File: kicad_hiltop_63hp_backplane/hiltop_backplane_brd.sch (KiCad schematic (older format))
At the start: 0 parts

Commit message: PCI EXPRESS 96
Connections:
- wire segments 43 -> 53
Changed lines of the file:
@@
 	1600 6300 1600 6400
 $Comp
-L power:GND #PWR?
+L power:GND #PWR02
 U 1 1 5D0E934B
 P 1600 2600
-F 0 "#PWR?" H 1600 2350 50  0001 C CNN
+F 0 "#PWR02" H 1600 2350 50  0001 C CNN
 F 1 "GND" H 1600 2450 50  0000 C CNN
 F 2 "" H 1600 2600 50  0001 C CNN
@@
 F48 "LED6" I R 3700 2350 39
 F49 "LED7" I R 3700 2400 39
-$EndSheet
-$Sheet
-S 1700 3100 2000 2050
-U 5C074E5E
-F0 "MotherBoard_Connector" 60
-F1 "MotherBoard_Connector.sch" 60
-$EndSheet
-$Sheet
-S 8150 600  1750 5800
-U 5A0778ED
-F0 "backplane_connector" 60
-F1 "backplane_connector.sch" 60
-F2 "EXT_RESET" I L 8150 2350 39
-F3 "LVDS_D1-" I L 8150 2300 39
-F4 "LVDS_D2-" I L 8150 2200 39
-F5 "LVDS_D3-" I L 8150 2100 39
-F6 "LVDS_D4-" I L 8150 2000 39
-F7 "LVDS_D5-" I L 8150 1900 39
-F8 "LVDS_D6-" I L 8150 1800 39
-F9 "LVDS_D7-" I L 8150 1700 39
-F10 "LVDS_D8-" I L 8150 1600 39
-F11 "LVDS_D9-" I L 8150 1500 39
-F12 "LVDS_D10-" I L 8150 1400 39
-F13 "LVDS_D11-" I L 8150 1300 39
-F14 "LVDS_D12-" I L 8150 1200 39
-F15 "LVDS_D12+" I L 8150 1150 39
-F16 "LVDS_D11+" I L 8150 1250 39
-F17 "LVDS_D10+" I L 8150 1350 39
-F18 "LVDS_D9+" I L 8150 1450 39
-F19 "LVDS_D8+" I L 8150 1550 39
-F20 "LVDS_D7+" I L 8150 1650 39
-F21 "LVDS_D6+" I L 8150 1750 39
-F22 "LVDS_D5+" I L 8150 1850 39
-F23 "LVDS_D4+" I L 8150 1950 39
-F24 "LVDS_D3+" I L 8150 2050 39
-F25 "LVDS_D2+" I L 8150 2150 39
-F26 "LVDS_D1+" I L 8150 2250 39
-F27 "LVPECLK+" I L 8150 650 39
-F28 "LVDSCLK-" I L 8150 700 39
-F29 "LVDS_D13-" I L 8150 1100 39
-F30 "LVDS_D13+" I L 8150 1050 39
-F31 "LVDS_D14-" I L 8150 1000 39
-F32 "LVDS_D14+" I L 8150 950 39
-F33 "LVDS_D15-" I L 8150 900 39
-F34 "LVDS_D15+" I L 8150 850 39
-F35 "LVDS_D16-" I L 8150 800 39
-F36 "LVDS_D16+" I L 8150 750 39
-F37 "GND" I R 9900 3900 39
 $EndSheet
 $Sheet
@@
 Wire Wire Line
 	7100 2300 8150 2300
+Wire Wire Line
+	7100 2475 8150 2475
+Wire Wire Line
+	7100 2525 8150 2525
+Wire Wire Line
+	7100 2575 8150 2575
+Wire Wire Line
+	7100 2625 8150 2625
+Wire Wire Line
+	7100 2675 8150 2675
+Wire Wire Line
+	7100 2725 8150 2725
+Wire Wire Line
+	7100 2775 8150 2775
+Wire Wire Line
+	7100 2825 8150 2825
+$Sheet
+S 8150 600  1750 5800
+U 5A0778ED
+F0 "backplane_connector" 60
+F1 "backplane_connector.sch" 60
+F2 "EXT_RESET" I L 8150 2350 39
+F3 "LVDS_D1-" I L 8150 2300 39
+F4 "LVDS_D2-" I L 8150 2200 39
+F5 "LVDS_D3-" I L 8150 2100 39
+F6 "LVDS_D4-" I L 8150 2000 39
+F7 "LVDS_D5-" I L 8150 1900 39
+F8 "LVDS_D6-" I L 8150 1800 39
+F9 "LVDS_D7-" I L 8150 1700 39
+F10 "LVDS_D8-" I L 8150 1600 39
+F11 "LVDS_D9-" I L 8150 1500 39
+F12 "LVDS_D10-" I L 8150 1400 39
+F13 "LVDS_D11-" I L 8150 1300 39
+F14 "LVDS_D12-" I L 8150 1200 39
+F15 "LVDS_D12+" I L 8150 1150 39
+F16 "LVDS_D11+" I L 8150 1250 39
+F17 "LVDS_D10+" I L 8150 1350 39
+F18 "LVDS_D9+" I L 8150 1450 39
+F19 "LVDS_D8+" I L 8150 1550 39
+F20 "LVDS_D7+" I L 8150 1650 39
+F21 "LVDS_D6+" I L 8150 1750 39
+F22 "LVDS_D5+" I L 8150 1850 39
+F23 "LVDS_D4+" I L 8150 1950 39
+F24 "LVDS_D3+" I L 8150 2050 39
+F25 "LVDS_D2+" I L 8150 2150 39
+F26 "LVDS_D1+" I L 8150 2250 39
+F27 "LVDS_D13-" I L 8150 1100 39
+F28 "LVDS_D13+" I L 8150 1050 39
+F29 "LVDS_D14-" I L 8150 1000 39
+F30 "LVDS_D14+" I L 8150 950 39
+F31 "LVDS_D15-" I L 8150 900 39
+F32 "LVDS_D15+" I L 8150 850 39
+F33 "LVDS_D16-" I L 8150 800 39
+F34 "LVDS_D16+" I L 8150 750 39
+F35 "GND" I R 9900 6250 39
+F36 "LVPECLK+" I L 8150 650 39
+F37 "LVDSCLK-" I L 8150 700 39
+F38 "FPGA_GPIO1" I L 8150 2475 39
+F39 "FPGA_GPIO2" I L 8150 2525 39
+F40 "FPGA_GPIO3" I L 8150 2575 39
+F41 "FPGA_GPIO4" I L 8150 2625 39
+F42 "FPGA_GPIO5" I L 8150 2675 39
+F43 "FPGA_GPIO6" I L 8150 2725 39
+F44 "FPGA_GPIO7" I L 8150 2775 39
+F45 "FPGA_GPIO8" I L 8150 2825 39
+F46 "FPGA_GPIO9" I L 8150 2900 39
+F47 "FPGA_GPIO10" I L 8150 2950 39
+F48 "MBRD_GPIO8" I R 9900 2825 39
+F49 "MBRD_GPIO9" I R 9900 2900 39
+F50 "MBRD_GPIO10" I R 9900 2950 39
+F51 "LCOM1" I L 8150 5450 39
+F52 "LCOM2" I L 8150 5500 39
+F53 "LCOM3" I L 8150 5550 39
+F54 "LCOM4" I L 8150 5600 39
+F55 "LCOM5" I L 8150 5650 39
+F56 "LCOM6" I L 8150 5700 39
+F57 "LCOM7" I L 8150 5750 39
+F58 "LCOM8" I L 8150 5800 39
+F59 "RCOM1" I R 9900 5450 39
+F60 "RCOM2" I R 9900 5500 39
+F61 "RCOM3" I R 9900 5550 39
+F62 "RCOM4" I R 9900 5600 39
+F63 "RCOM5" I R 9900 5650 39
+F64 "RCOM6" I R 9900 5700 39
+F65 "RCOM7" I R 9900 5750 39
+F66 "RCOM8" I R 9900 5800 39
+F67 "USB_N" I L 8150 6275 39
+F68 "USB_P" I L 8150 6225 39
+F69 "FPGA_GPIO11" I L 8150 3000 39
+F70 "FPGA_GPIO12" I L 8150 3050 39
+F71 "FPGA_GPIO13" I L 8150 3100 39
+F72 "FPGA_GPIO14" I L 8150 3150 39
+F73 "FPGA_GPIO15" I L 8150 3200 39
+F74 "FPGA_GPIO16" I L 8150 3250 39
+F75 "FPGA_GPIO17" I L 8150 3325 39
+F76 "FPGA_GPIO18" I L 8150 3375 39
+F77 "FPGA_GPIO19" I L 8150 3425 39
+F78 "FPGA_GPIO20" I L 8150 3475 39
+F79 "FPGA_GPIO21" I L 8150 3525 39
+F80 "FPGA_GPIO22" I L 8150 3575 39
+F81 "FPGA_GPIO23" I L 8150 3625 39
+F82 "FPGA_GPIO24" I L 8150 3675 39
+F83 "FPGA_GPIO25" I L 8150 3750 39
+F84 "FPGA_GPIO26" I L 8150 3800 39
+F85 "FPGA_GPIO27" I L 8150 3850 39
+F86 "FPGA_GPIO28" I L 8150 3900 39
+F87 "FPGA_GPIO29" I L 8150 3950 39
+F88 "FPGA_GPIO30" I L 8150 4000 39
+F89 "+12V0" I R 9900 675 39
+F90 "+5V0" I R 9900 725 39
+F91 "+3V3V" I R 9900 825 39
+F92 "-5V0" I R 9900 775 39
+F93 "V_ADJ" I R 9900 875 39
+F94 "I2C0_SDA" I R 9900 1875 39
+F95 "I2C0_SCL" I R 9900 1925 39
+F96 "I2C1_SDA" I R 9900 1975 39
+F97 "I2C1_SCL" I R 9900 2025 39
+F98 "MBRD_GPIO1" I R 9900 2475 39
+F99 "MBRD_GPIO2" I R 9900 2525 39
+F100 "MBRD_GPIO3" I R 9900 2575 39
+F101 "MBRD_GPIO4" I R 9900 2625 39
+F102 "MBRD_GPIO5" I R 9900 2675 39
+F103 "MBRD_GPIO6" I R 9900 2725 39
+F104 "MBRD_GPIO7" I R 9900 2775 39
+F105 "MBRD_GPIO14" I R 9900 3150 39
+F106 "MBRD_GPIO15" I R 9900 3200 39
+F107 "MBRD_GPIO16" I R 9900 3250 39
+F108 "MBRD_GPIO17" I R 9900 3325 39
+F109 "MBRD_GPIO24" I R 9900 3675 39
+F110 "MBRD_GPIO25" I R 9900 3750 39
+F111 "MBRD_GPIO26" I R 9900 3800 39
+F112 "MBRD_GPIO27" I R 9900 3850 39
+F113 "MBRD_GPIO11" I R 9900 3000 39
+F114 "MBRD_GPIO12" I R 9900 3050 39
+F115 "MBRD_GPIO13" I R 9900 3100 39
+F116 "MBRD_GPIO21" I R 9900 3525 39
+F117 "MBRD_GPIO22" I R 9900 3575 39
+F118 "MBRD_GPIO23" I R 9900 3625 39
+F119 "MBRD_GPIO18" I R 9900 3375 39
+F120 "MBRD_GPIO19" I R 9900 3425 39
+F121 "MBRD_GPIO20" I R 9900 3475 39
+F122 "MBRD_GPIO28" I R 9900 3900 39
+F123 "MBRD_GPIO29" I R 9900 3950 39
+F124 "MBRD_GPIO30" I R 9900 4000 39
+F125 "SPI0_MOSI" I R 9900 1325 39
+F126 "SPI0_MISO" I R 9900 1375 39
+F127 "SPI0_SCK" I R 9900 1425 39
+F128 "SPI0_CS0" I R 9900 1475 39
+F129 "SPI0_CS1" I R 9900 1525 39
+F130 "SPI1_MOSI" I R 9900 1600 39
+F131 "SPI1_MISO" I R 9900 1650 39
+F132 "SPI1_SCK" I R 9900 1700 39
+F133 "SPI1_CS0" I R 9900 1750 39
+F134 "SPI1_CS1" I R 9900 1800 39
+F135 "RESET" I R 9900 4075 39
+F136 "SHUTDOWN" I R 9900 4125 39
+F137 "PSEL_0" I R 9900 4175 39
+F138 "SYS_TRIG_0" I R 9900 4350 39
+F139 "SYS_CLK_0" I R 9900 4400 39
+F140 "PSEL_1" I R 9900 4225 39
+F141 "SYS_TRIG_1" I R 9900 4450 39
+F142 "SYS_CLK_1" I R 9900 4500 39
+F143 "PSEL_2" I R 9900 4275 39
+F144 "SYS_TRIG_2" I R 9900 4550 39
+F145 "SYS_CLK_2" I R 9900 4600 39
+F146 "RESERVED_3" I L 8150 5875 39
+F147 "RESERVED_2" I L 8150 5925 39
+F148 "RESERVED_1" I L 8150 5975 39
+F149 "PWM0" I L 8150 5050 39
+F150 "PWM1" I L 8150 5100 39
+F151 "PWM2" I L 8150 5150 39
+F152 "PWM3" I L 8150 5200 39
+F153 "PWM4" I L 8150 5250 39
+F154 "PWM6" I L 8150 5350 39
+F155 "PWM5" I L 8150 5300 39
+$EndSheet
+Wire Wire Line
+	9900 6250 10025 6250
+Wire Wire Line
+	10025 6250 10025 6325
+$Comp
+L power:GND #PWR?
+U 1 1 603510FC
+P 10025 6325
+F 0 "#PWR?" H 10025 6075 50  0001 C CNN
+F 1 "GND" H 10030 6152 50  0000 C CNN
+F 2 "" H 10025 6325 50  0001 C CNN
+F 3 "" H 10025 6325 50  0001 C CNN
+	1    10025 6325
+	1    0    0    -1
+$EndComp
+$Sheet
+S 1700 3100 2000 2050
+U 5C074E5E
+F0 "MotherBoard_Connector" 60
+F1 "MotherBoard_Connector.sch" 60
+F2 "MBRD_USB_P" I L 1700 3175 39
+F3 "MBRD_USB_N" I L 1700 3225 39
+F4 "MBRD_GPIO11" I R 3700 3650 60
+F5 "MBRD_GPIO12" I R 3700 3700 60
+F6 "MBRD_GPIO13" I R 3700 3750 60
+F7 "MBRD_GPIO14" I R 3700 3800 60
+F8 "MBRD_GPIO15" I R 3700 3850 60
+F9 "MBRD_GPIO16" I R 3700 3900 60
+F10 "MBRD_I2C0_SDA" I L 1700 3300 39
+F11 "MBRD_I2C1_SDA" I L 1700 3400 39
+F12 "MBRD_I2C0_SCL" I L 1700 3350 39
+F13 "MBRD_I2C1_SCL" I L 1700 3450 39
+F14 "MBRD_RST" I L 1700 3550 39
+F15 "MBRD_SHUTDOWN" I L 1700 3600 39
+F16 "MBRD_PWM0" I L 1700 4400 39
+F17 "MBRD_PWM1" I L 1700 4450 39
+F18 "MBRD_GPIO1" I R 3700 3150 60
+F19 "MBRD_GPIO2" I R 3700 3200 60
+F20 "MBRD_GPIO3" I R 3700 3250 60
+F21 "MBRD_GPIO4" I R 3700 3300 60
+F22 "MBRD_GPIO5" I R 3700 3350 60
+F23 "MBRD_GPIO6" I R 3700 3400 60
+F24 "MBRD_GPIO7" I R 3700 3450 60
+F25 "MBRD_PWM8" I R 3700 3500 60
+F26 "MBRD_PWM9" I R 3700 3550 60
+F27 "MBRD_PWM10" I R 3700 3600 60
+F28 "MBRD_SPI1_MOSI" I L 1700 3825 39
+F29 "MBRD_SPI1_MISO" I L 1700 3875 39
+F30 "MBRD_SPI1_SCK" I L 1700 3925 39
+F31 "MBRD_SPI1_CS0" I L 1700 3975 39
+F32 "MBRD_SPI1_CS1" I L 1700 4050 39
+F33 "MBRD_SPI0_MOSI" I L 1700 4100 39
+F34 "MBRD_SPI0_MISO" I L 1700 4150 39
+F35 "MBRD_SPI0_SCK" I L 1700 4200 39
+F36 "MBRD_SPI0_CS0" I L 1700 4250 39
+F37 "MBRD_SPI0_CS1" I L 1700 4300 39
+F38 "MBRD_RESERVED_0" I L 1700 4875 60
+F39 "MBRD_RESERVED_1" I L 1700 4950 60
+F40 "MBRD_RESERVED_2" I L 1700 5025 60
+F41 "MBRD_RESERVED_3" I L 1700 5075 60
+F42 "MBRD_PSEL_0" I L 1700 3650 39
+F43 "MBRD_PSEL_1" I L 1700 3700 39
+F44 "MBRD_PSEL_2" I L 1700 3750 39
+F45 "MBRD_PSEL_3" I L 1700 3775 60
+F46 "MBRD_PSEL_4" I R 3700 4375 60
+F47 "MBRD_PSEL_5" I R 3700 4450 60
+F48 "MBRD_SYC_CLK" I R 3700 4525 60
+F49 "MBRD_SYS_TRIG" I R 3700 4600 60
+F50 "+12V" I R 3700 4750 60
+F51 "+5V" I R 3700 4825 60
+F52 "+3V3" I R 3700 4900 60
+F53 "-5V" I R 3700 5000 60
+F54 "+2V5" I R 3700 5075 60
+F55 "+1V8" I R 3700 4675 60
+F56 "+1V2" I R 3700 4950 60
+F57 "VADJ_DC" I R 3700 5125 60
+F58 "+3V3_IN" I R 3700 4275 60
+F59 "CON_SDA3" I R 3700 4175 60
+F60 "CON_SCL3" I R 3700 4100 60
+$EndSheet
 $EndSCHEMATC

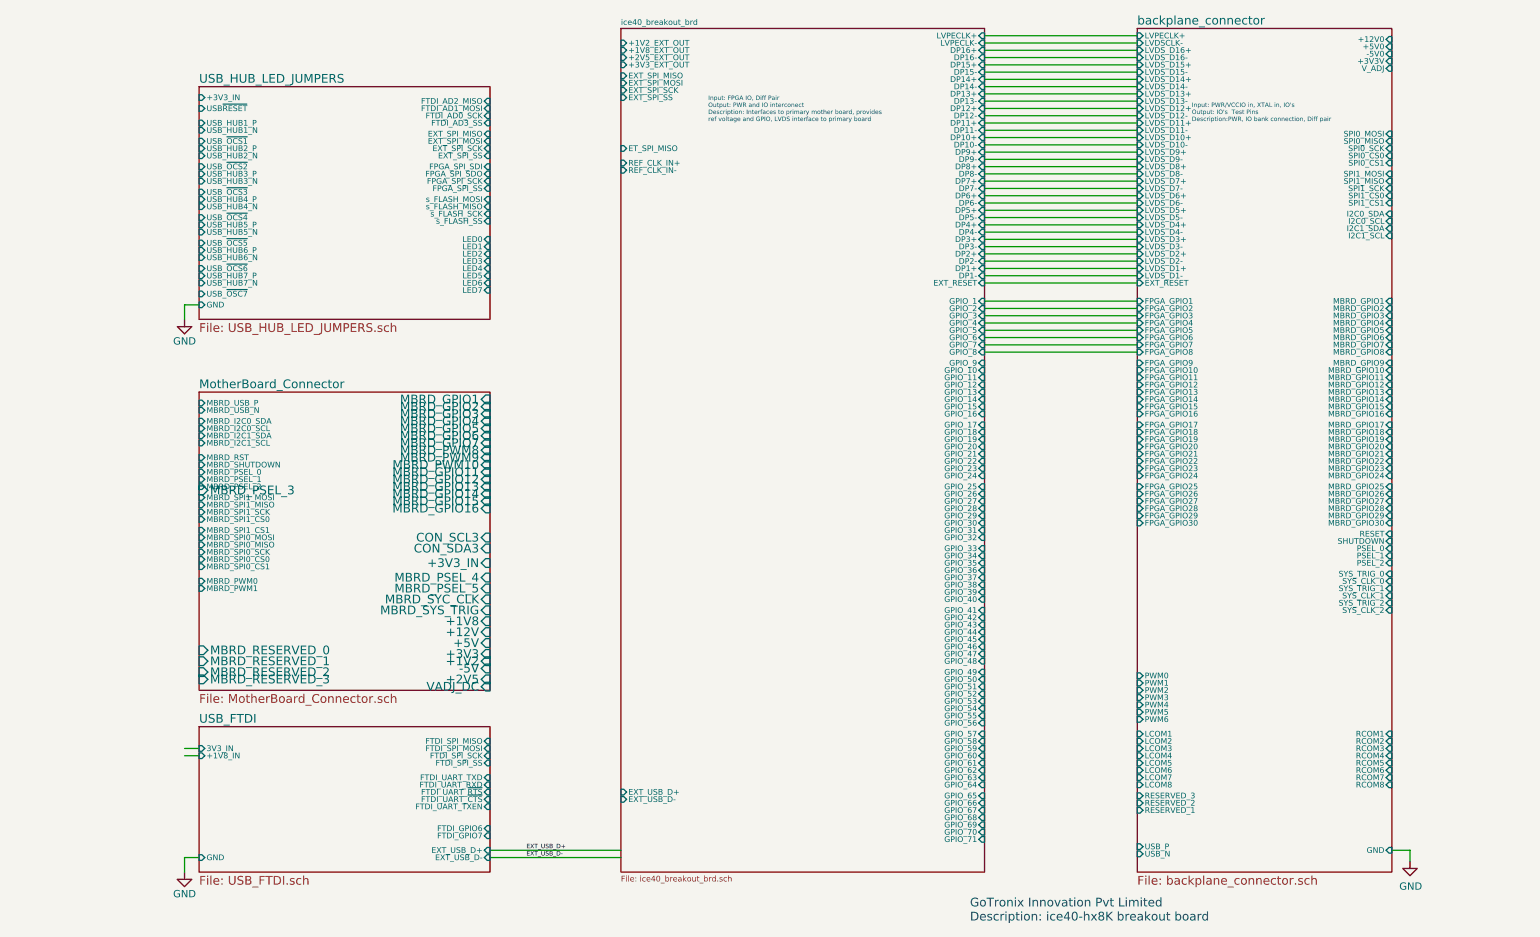
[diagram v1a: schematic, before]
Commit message: back plane connector update
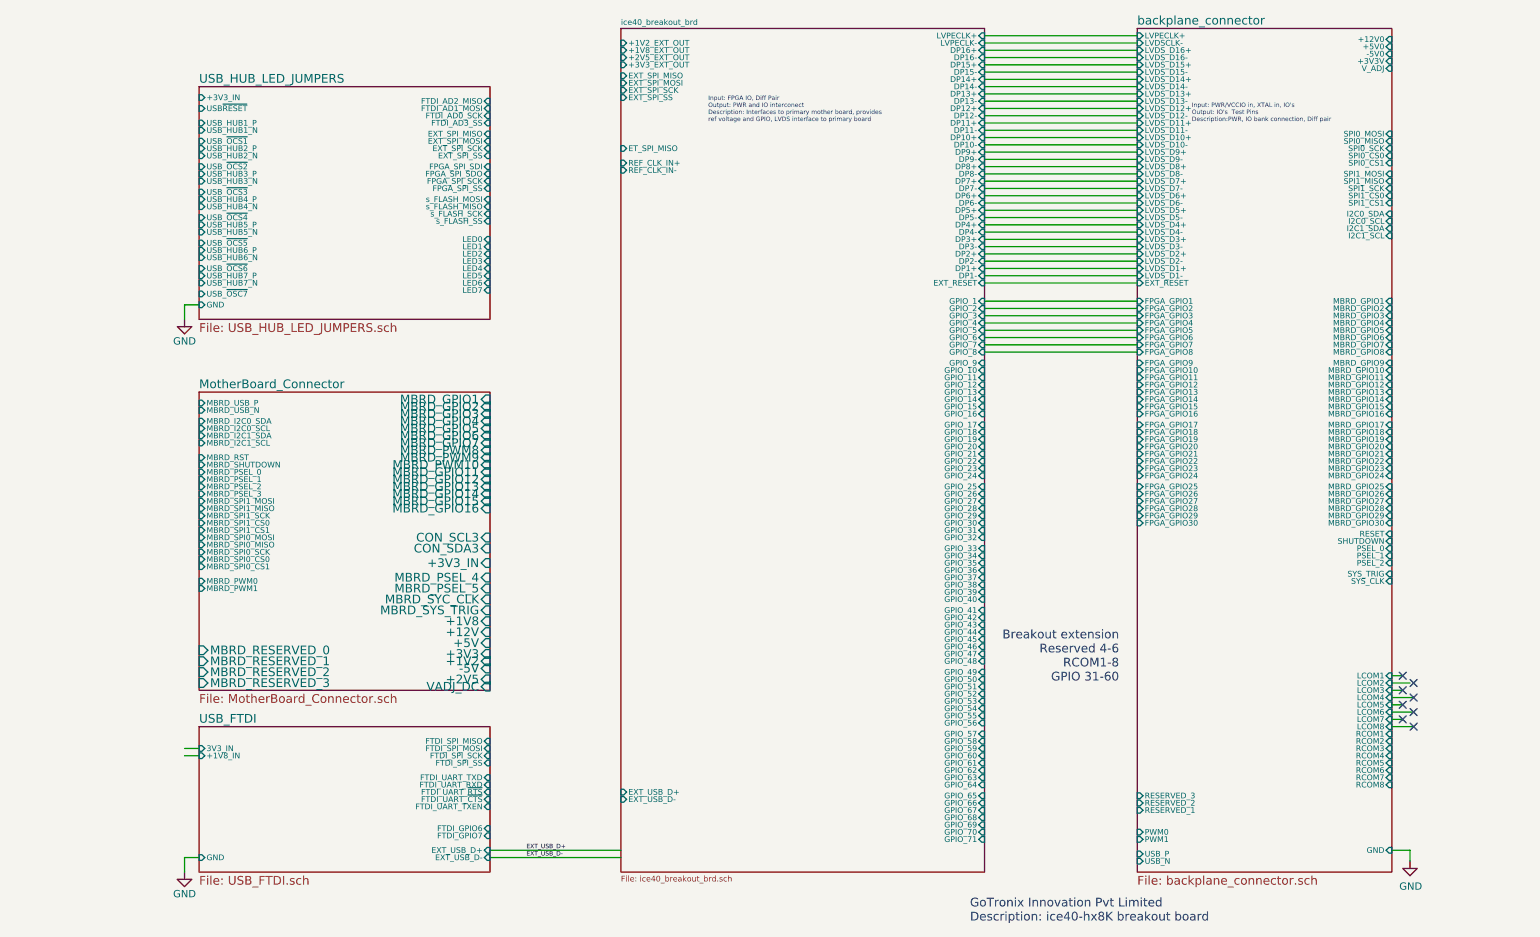
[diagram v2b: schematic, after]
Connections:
- wire segments 53 -> 61
- no-connect marks 0 -> 8
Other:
- note added: "Breakout extension\nReserved 4-6\nRCOM1-8 \nGPIO 31-60"
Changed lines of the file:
@@
 F49 "MBRD_GPIO9" I R 9900 2900 39
 F50 "MBRD_GPIO10" I R 9900 2950 39
-F51 "LCOM1" I L 8150 5450 39
-F52 "LCOM2" I L 8150 5500 39
-F53 "LCOM3" I L 8150 5550 39
-F54 "LCOM4" I L 8150 5600 39
-F55 "LCOM5" I L 8150 5650 39
-F56 "LCOM6" I L 8150 5700 39
-F57 "LCOM7" I L 8150 5750 39
-F58 "LCOM8" I L 8150 5800 39
+F51 "LCOM1" I R 9900 5050 39
+F52 "LCOM2" I R 9900 5100 39
+F53 "LCOM3" I R 9900 5150 39
+F54 "LCOM4" I R 9900 5200 39
+F55 "LCOM5" I R 9900 5250 39
+F56 "LCOM6" I R 9900 5300 39
+F57 "LCOM7" I R 9900 5350 39
+F58 "LCOM8" I R 9900 5400 39
 F59 "RCOM1" I R 9900 5450 39
 F60 "RCOM2" I R 9900 5500 39
@@
 F65 "RCOM7" I R 9900 5750 39
 F66 "RCOM8" I R 9900 5800 39
-F67 "USB_N" I L 8150 6275 39
-F68 "USB_P" I L 8150 6225 39
+F67 "USB_N" I L 8150 6325 39
+F68 "USB_P" I L 8150 6275 39
 F69 "FPGA_GPIO11" I L 8150 3000 39
 F70 "FPGA_GPIO12" I L 8150 3050 39
@@
 F136 "SHUTDOWN" I R 9900 4125 39
 F137 "PSEL_0" I R 9900 4175 39
-F138 "SYS_TRIG_0" I R 9900 4350 39
-F139 "SYS_CLK_0" I R 9900 4400 39
+F138 "SYS_TRIG" I R 9900 4350 39
+F139 "SYS_CLK" I R 9900 4400 39
 F140 "PSEL_1" I R 9900 4225 39
-F141 "SYS_TRIG_1" I R 9900 4450 39
-F142 "SYS_CLK_1" I R 9900 4500 39
-F143 "PSEL_2" I R 9900 4275 39
-F144 "SYS_TRIG_2" I R 9900 4550 39
-F145 "SYS_CLK_2" I R 9900 4600 39
-F146 "RESERVED_3" I L 8150 5875 39
-F147 "RESERVED_2" I L 8150 5925 39
-F148 "RESERVED_1" I L 8150 5975 39
-F149 "PWM0" I L 8150 5050 39
-F150 "PWM1" I L 8150 5100 39
-F151 "PWM2" I L 8150 5150 39
-F152 "PWM3" I L 8150 5200 39
-F153 "PWM4" I L 8150 5250 39
-F154 "PWM6" I L 8150 5350 39
-F155 "PWM5" I L 8150 5300 39
+F141 "PSEL_2" I R 9900 4275 39
+F142 "RESERVED_3" I L 8150 5875 39
+F143 "RESERVED_2" I L 8150 5925 39
+F144 "RESERVED_1" I L 8150 5975 39
+F145 "PWM0" I L 8150 6125 39
+F146 "PWM1" I L 8150 6175 39
 $EndSheet
 Wire Wire Line
@@
 F26 "MBRD_PWM9" I R 3700 3550 60
 F27 "MBRD_PWM10" I R 3700 3600 60
-F28 "MBRD_SPI1_MOSI" I L 1700 3825 39
-F29 "MBRD_SPI1_MISO" I L 1700 3875 39
-F30 "MBRD_SPI1_SCK" I L 1700 3925 39
-F31 "MBRD_SPI1_CS0" I L 1700 3975 39
+F28 "MBRD_SPI1_MOSI" I L 1700 3850 39
+F29 "MBRD_SPI1_MISO" I L 1700 3900 39
+F30 "MBRD_SPI1_SCK" I L 1700 3950 39
+F31 "MBRD_SPI1_CS0" I L 1700 4000 39
 F32 "MBRD_SPI1_CS1" I L 1700 4050 39
 F33 "MBRD_SPI0_MOSI" I L 1700 4100 39
@@
 F39 "MBRD_RESERVED_1" I L 1700 4950 60
 F40 "MBRD_RESERVED_2" I L 1700 5025 60
-F41 "MBRD_RESERVED_3" I L 1700 5075 60
+F41 "MBRD_RESERVED_3" I L 1700 5100 60
 F42 "MBRD_PSEL_0" I L 1700 3650 39
 F43 "MBRD_PSEL_1" I L 1700 3700 39
 F44 "MBRD_PSEL_2" I L 1700 3750 39
-F45 "MBRD_PSEL_3" I L 1700 3775 60
+F45 "MBRD_PSEL_3" I L 1700 3800 39
 F46 "MBRD_PSEL_4" I R 3700 4375 60
 F47 "MBRD_PSEL_5" I R 3700 4450 60
@@
 F60 "CON_SCL3" I R 3700 4100 60
 $EndSheet
+NoConn ~ 9975 5050
+NoConn ~ 10050 5100
+NoConn ~ 9975 5150
+NoConn ~ 10050 5200
+NoConn ~ 9975 5250
+NoConn ~ 10050 5300
+NoConn ~ 9975 5350
+NoConn ~ 10050 5400
+Wire Wire Line
+	9975 5050 9900 5050
+Wire Wire Line
+	10025 5100 9900 5100
+Wire Wire Line
+	9975 5150 9900 5150
+Wire Wire Line
+	10050 5200 9900 5200
+Wire Wire Line
+	9975 5250 9900 5250
+Wire Wire Line
+	10050 5300 9900 5300
+Wire Wire Line
+	9900 5350 9975 5350
+Wire Wire Line
+	10050 5400 9900 5400
+Text Notes 8025 5100 2    60   ~ 0
+Breakout extension\nReserved 4-6\nRCOM1-8 \nGPIO 31-60
 $EndSCHEMATC

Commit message: first pass draft for review
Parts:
- added TP? (x13): TestPoint, symbol Connector:TestPoint
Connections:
- net labels added: +12V, +1V2, +1V8, +2V5, +3V3, +5V, -5V, CDONE, CLK, CRST, I2C0_SCL, I2C0_SDA, I2C1_SCL, I2C1_SDA, LED0, LED1, LED2, LED3, LED4, PSEL0, PSEL1, PSEL2, PWM0, PWM1, RST, SHUTDOWN, SPI0_CS0, SPI0_CS1, SPI0_MISO, SPI0_MOSI, SPI0_SCK, SPI1_CS0, SPI1_CS1, SPI1_CS2, SPI1_MISO, SPI1_MOSI, SPI1_SCK, TRIG, UART_TXEN, USB1_N, USB1_P, USB2_N, USB2_P, USB3_N, USB3_P, USB_DN, USB_DP, USB_RST, VADJ
- net labels removed: EXT_USB_D+, EXT_USB_D-
- wire segments 61 -> 266
- no-connect marks 8 -> 23
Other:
- note added: "CHECK IF GPIO PIN UNUSED\n REPURPOSE FOR LEDS"
- note added: "CHECK IF MOTHERBOARD \nSENDS REF CLK TO FPGA"
- note added: "REPURPOSE GPIO 49-52 \nFOR FLASH SPI - CHECK"
- note added: "REPURPOSE GPIO 49-52 \nFOR FPGA SPI - CHECK"
- note removed: "Breakout extension\nReserved 4-6\nRCOM1-8 \nGPIO 31-60"
